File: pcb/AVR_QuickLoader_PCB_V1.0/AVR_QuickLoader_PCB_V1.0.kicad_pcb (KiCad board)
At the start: 4 copper layers, 15 parts, among them J1 USB_B, U1 CH340C, U2 ATmega328P-A, U3 ATmega328P-P, Y1 Crystal, Y2 Crystal

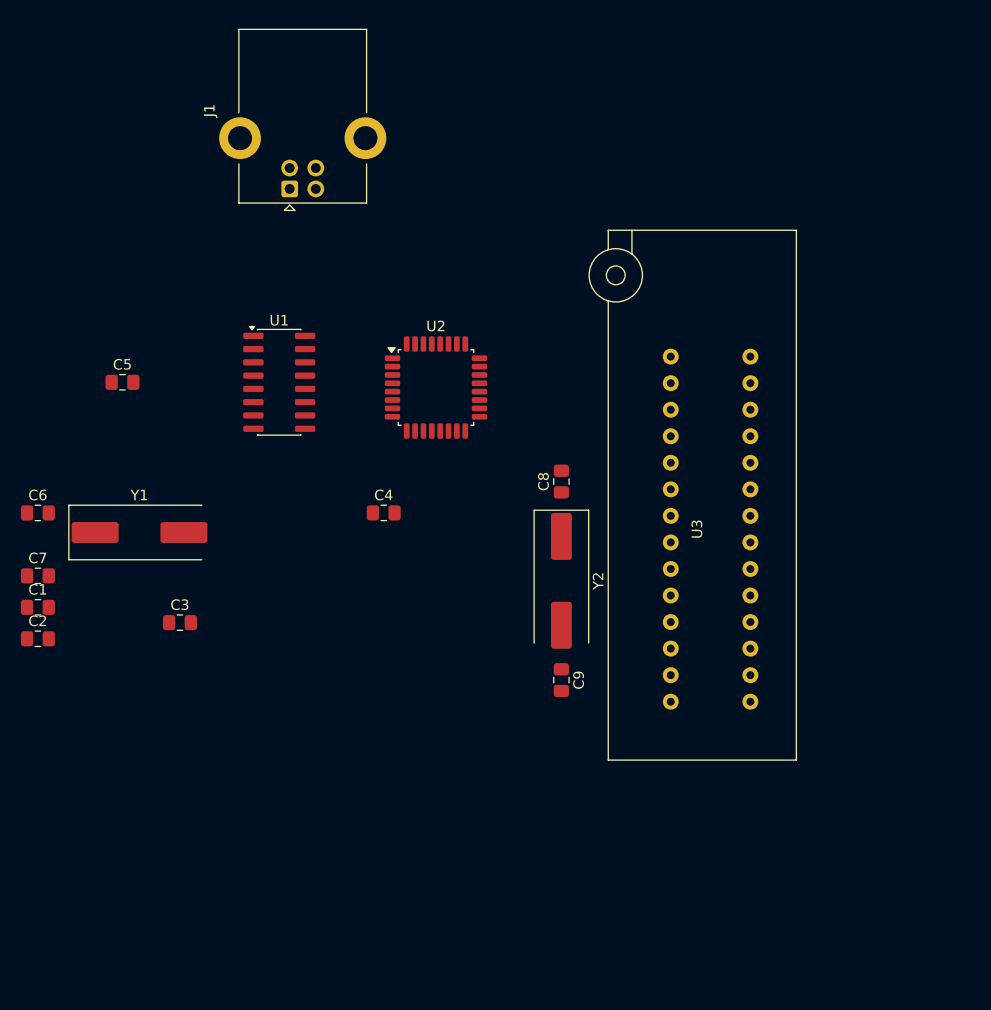
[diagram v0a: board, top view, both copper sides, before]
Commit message: added readme and started the pcb design routing
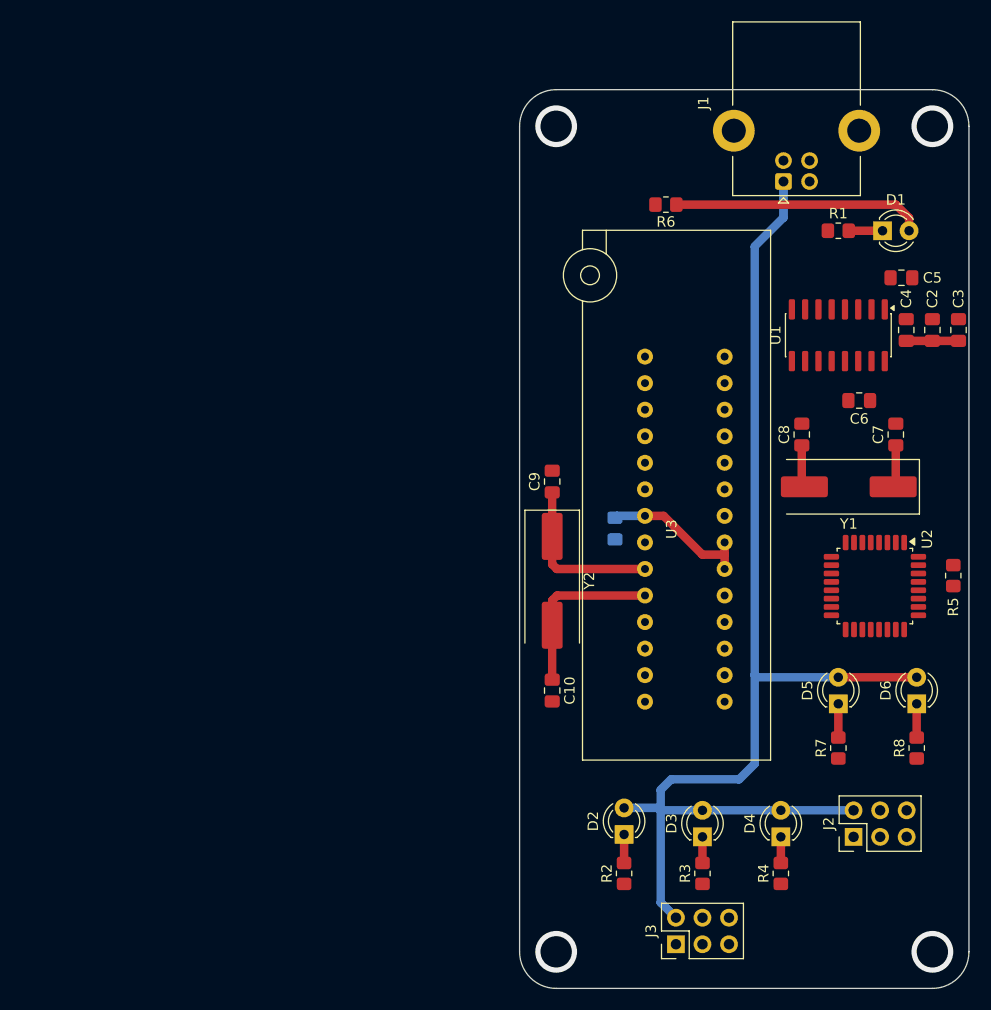
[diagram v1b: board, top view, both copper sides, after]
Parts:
- added C1: 100nF, Capacitor_SMD:C_0805_2012Metric_Pad1.18x1.45mm_HandSolder, B.Cu at (161.6, 91.0)
- added D1: LED, LED_THT:LED_D3.0mm, F.Cu at (187.2, 62.5)
- added D2: LED, LED_THT:LED_D3.0mm, F.Cu at (162.5, 120.3)
- added D3: LED, LED_THT:LED_D3.0mm, F.Cu at (170.0, 120.5)
- added D4: LED, LED_THT:LED_D3.0mm, F.Cu at (177.5, 120.5)
- added D5: LED, LED_THT:LED_D3.0mm, F.Cu at (183.0, 107.8)
- added D6: LED, LED_THT:LED_D3.0mm, F.Cu at (190.5, 107.8)
- added J2: ICSP, Connector_PinHeader_2.54mm:PinHeader_2x03_P2.54mm_Vertical, F.Cu at (184.5, 120.5)
- added J3: ICSP, Connector_PinHeader_2.54mm:PinHeader_2x03_P2.54mm_Vertical, F.Cu at (167.5, 130.8)
- added R1: 470, Resistor_SMD:R_0805_2012Metric_Pad1.20x1.40mm_HandSolder, F.Cu at (183.0, 62.5)
- added R2: 470, Resistor_SMD:R_0805_2012Metric_Pad1.20x1.40mm_HandSolder, F.Cu at (162.5, 124.0)
- added R3: 470, Resistor_SMD:R_0805_2012Metric_Pad1.20x1.40mm_HandSolder, F.Cu at (170.0, 124.0)
- added R4: 470, Resistor_SMD:R_0805_2012Metric_Pad1.20x1.40mm_HandSolder, F.Cu at (177.5, 124.0)
- added R5: 10K, Resistor_SMD:R_0805_2012Metric_Pad1.20x1.40mm_HandSolder, F.Cu at (194.0, 95.5)
- added R6: 10K, Resistor_SMD:R_0805_2012Metric_Pad1.20x1.40mm_HandSolder, F.Cu at (166.5, 60.0)
- added R7: 470, Resistor_SMD:R_0805_2012Metric_Pad1.20x1.40mm_HandSolder, F.Cu at (183.0, 112.0)
- added R8: 470, Resistor_SMD:R_0805_2012Metric_Pad1.20x1.40mm_HandSolder, F.Cu at (190.5, 112.0)
- moved C3 92.9 mm to (194.5, 72.0), turned to 90 degrees
- moved C2 89.6 mm to (192.0, 72.0), turned to 90 degrees
- moved C7 82.4 mm to (188.5, 82.0), turned to 90 degrees
- moved C4 74.9 mm to (189.5, 72.0), turned to 90 degrees
- moved C8 74.3 mm to (179.5, 82.0), turned to 90 degrees
- moved C6 70.5 mm to (185.0, 78.8)
- moved Y1 68.0 mm to (184.0, 87.0), turned to 180 degrees
- moved C5 54.4 mm to (189.0, 67.0), turned to 180 degrees
- moved U1 53.7 mm to (183.0, 72.5), turned to -90 degrees
- moved J1 47.3 mm to (177.8, 57.8)
- moved U2 46.1 mm to (186.5, 96.5), turned to -90 degrees
- moved U3 2.47 mm to (172.1, 91.1)
- moved C10 1.33 mm to (155.6, 106.5)
- moved C9 0.88 mm to (155.6, 86.5)
- moved Y2 0.88 mm to (155.6, 96.0)
- renumbered C9 to C10, C1 to C2, C2 to C3, C3 to C4, C4 to C5, C5 to C6, C6 to C7, C7 to C8, C8 to C9
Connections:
- C3 pad 1: Net-(J1-VBUS) -> +5V
- C4 pad 1: Net-(J1-VBUS) -> +5V
- J1 pad 1: Net-(J1-VBUS) -> +5V
- U1 pad 16: Net-(J1-VBUS) -> +5V
- U2 pad 14: unconnected-(U2-PB2-Pad14) -> /tUC_DTR
- U2 pad 15: unconnected-(U2-PB3-Pad15) -> /SPI_MOSI
- U2 pad 16: unconnected-(U2-PB4-Pad16) -> /SPI_MISO
- U2 pad 17: unconnected-(U2-PB5-Pad17) -> /SPI_CLK
- U2 pad 7: unconnected-(U2-XTAL1/PB6-Pad7) -> /pUC_OSC1
- U2 pad 8: unconnected-(U2-XTAL2/PB7-Pad8) -> /pUC_OSC2
- U3 pad 1: unconnected-(U3-~{RESET}/PC6-Pad1) -> /tUC_DTR
- U3 pad 17: unconnected-(U3-PB3-Pad17) -> /SPI_MOSI
- U3 pad 18: unconnected-(U3-PB4-Pad18) -> /SPI_MISO
- U3 pad 19: unconnected-(U3-PB5-Pad19) -> /SPI_CLK
- U3 pad 2: unconnected-(U3-PD0-Pad2) -> /tUC_TX
- U3 pad 3: unconnected-(U3-PD1-Pad3) -> /tUC_RX
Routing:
- net +5V: track 0.00 -> 161.1 mm
- net /tUC_OSC2: track 0.00 -> 16.7 mm
- net /tUC_OSC1: track 0.00 -> 15.9 mm
- net /pUC_OSC2: track 0.00 -> 4.07 mm
- net /pUC_OSC1: track 0.00 -> 4.07 mm
- net Net-(D6-K): track 0.00 -> 3.23 mm
- net Net-(D5-K): track 0.00 -> 3.23 mm
- net Net-(D1-K): track 0.00 -> 3.23 mm
- net Net-(D2-K): track 0.00 -> 2.73 mm
- net Net-(D4-K): track 0.00 -> 2.50 mm
- net Net-(D3-K): track 0.00 -> 2.50 mm
- net (no net): vias 0 -> 4
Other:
- board outline added: 43 x 86 mm
- copper layers 4 -> 2

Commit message: finished pcb design
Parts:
- moved C3 0.70 mm to (193.8, 72.0)
- moved C2 0.40 mm to (191.6, 72.0)
- moved R5 0.20 mm to (193.8, 95.5)
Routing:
- net /tUC_DTR: track 0.00 -> 126.9 mm, vias 0 -> 2
- net /SPI_MOSI: track 0.00 -> 106.1 mm, vias 0 -> 1
- net /SPI_CLK: track 0.00 -> 90.1 mm, vias 0 -> 3
- net /SPI_MISO: track 0.00 -> 87.8 mm, vias 0 -> 4
- net /pUC_RX: track 0.00 -> 73.9 mm, vias 0 -> 5
- net +5V: track 161.1 -> 231.1 mm
- net /pUC_TX: track 0.00 -> 63.4 mm, vias 0 -> 3
- net GND: track 0.00 -> 43.9 mm, vias 0 -> 5
- net /pUC_DTR: track 0.00 -> 31.5 mm, vias 0 -> 2
- net Net-(J1-D+): track 0.00 -> 16.1 mm, vias 0 -> 1
- net Net-(J1-D-): track 0.00 -> 12.6 mm, vias 0 -> 1
- net Net-(U1-V3): track 0.00 -> 9.84 mm
- net /pUC_OSC2: track 4.07 -> 12.5 mm
- net /pUC_OSC1: track 4.07 -> 12.4 mm
- net Net-(U1-~{DTR}): track 0.00 -> 3.91 mm
- added copper zone on B.Cu, net GND
- added copper zone on F.Cu, net GND

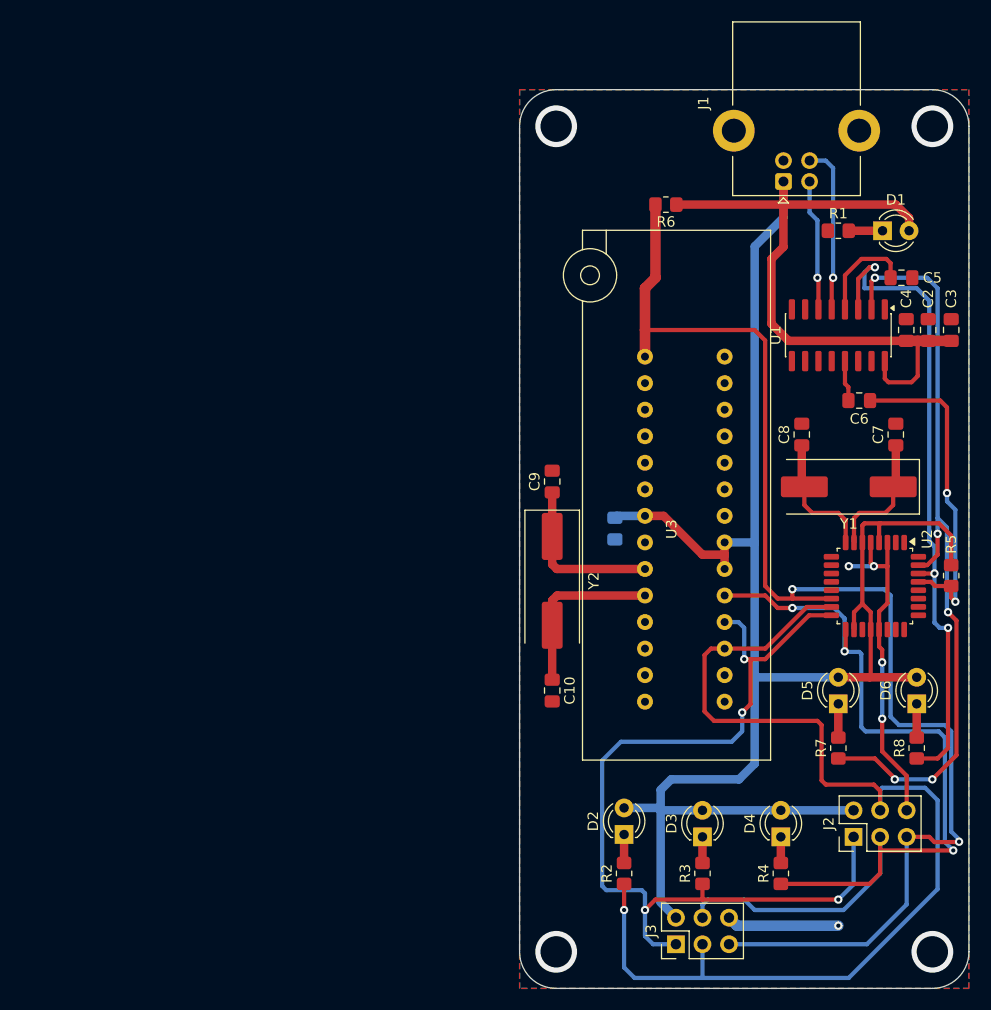
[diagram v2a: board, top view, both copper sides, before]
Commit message: refactored the arrangement on the SCH file
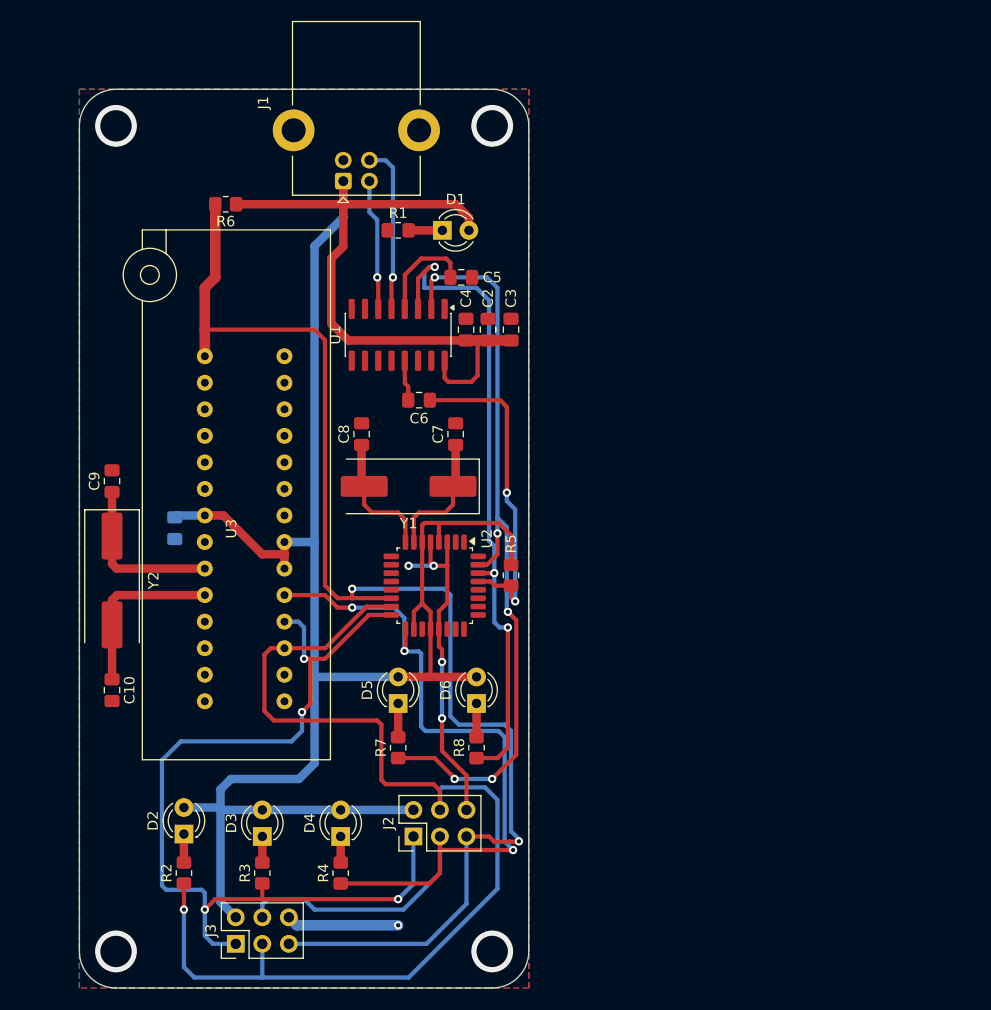
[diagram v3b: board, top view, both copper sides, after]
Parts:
- moved C1 42.1 mm to (119.5, 91.0)
- moved C10 42.1 mm to (113.5, 106.5)
- moved C2 42.1 mm to (149.5, 72.0)
- moved C3 42.1 mm to (151.7, 72.0)
- moved C4 42.1 mm to (147.4, 72.0)
- moved C5 42.1 mm to (146.9, 67.0)
- moved C6 42.1 mm to (142.9, 78.7)
- moved C7 42.1 mm to (146.4, 82.0)
- moved C8 42.1 mm to (137.4, 82.0)
- moved C9 42.1 mm to (113.5, 86.5)
- moved D2 42.1 mm to (120.4, 120.2)
- moved D3 42.1 mm to (127.9, 120.5)
- moved D4 42.1 mm to (135.4, 120.5)
- moved D5 42.1 mm to (140.9, 107.7)
- moved D6 42.1 mm to (148.4, 107.7)
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
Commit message: Updates AVR QuickLoader PCB project
Includes new project backup archives and reflects an update to the project's internal history. Also adjusts KiCad project preferences, setting a new active layer and clearing the layer preset.
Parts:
- added G***: LOGO, KennyNeutron:JuanRobotix_LOGO_12x12, F.Cu at (141.4, 129.3)
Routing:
- net GND: track 43.9 -> 38.8 mm
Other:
- board text added: "AVR QuickLoader V1.0"
- board text added: "By: KennyNeutron"
